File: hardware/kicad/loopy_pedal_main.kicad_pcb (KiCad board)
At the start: 2 copper layers, 80 x 66 mm, 76 parts, among them J1 USB_C_Receptacle_USB2.0_16P, J10 Conn_01x02, J11 Conn_01x03, J2 Barrel_Jack, J3 Conn_01x06, J4 Conn_01x06, J5 Conn_01x08, J6 Conn_02x03_Odd_Even, J7 Conn_02x03_Odd_Even, J8 DIN-5_180degree, J9 DIN-5_180degree, Q1 AO3401A, SW1 SW_Push, SW2 SW_Push, U1 ATmega328P-A, U10 74AHCT1G08, U2 ATmega16U2-A, U3 AP63203WU, U4 74AHCT1G125, U5 LM66100DCK, U6 LM66100DCK, U7 USBLC6-2SC6, U8 74AHCT1G125, U9 H11L1, Y1 16MHz, Y2 16MHz

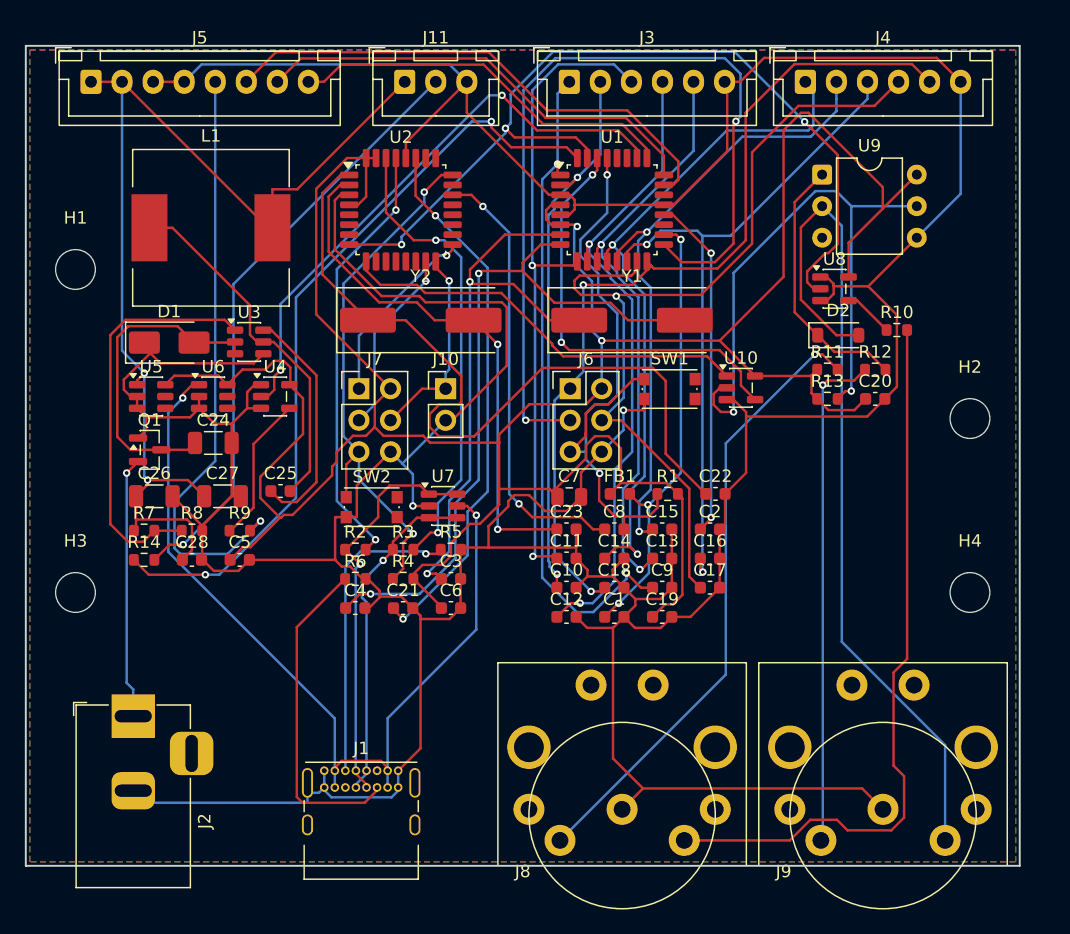
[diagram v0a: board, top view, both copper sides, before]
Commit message: fix(pcb): symmetric mounting holes, 82x66mm
Made the four M3 mounting holes a proper symmetric rectangle (74x26mm) instead
of the asymmetric set (a corner hole had been nudged to dodge the opto).
Widened 2mm to 82x66 to give the right-hand holes a clear column. Re-routed
clean: 0 DRC errors / 0 unrouted.
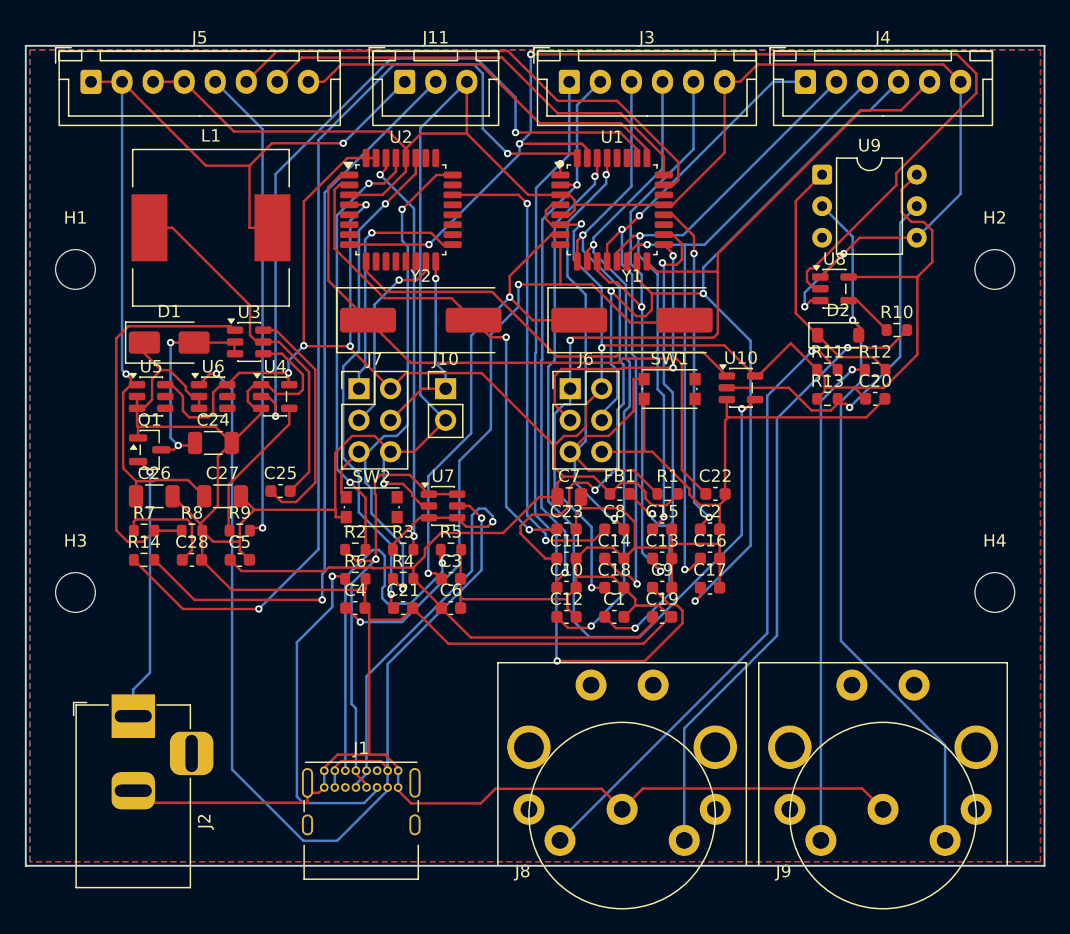
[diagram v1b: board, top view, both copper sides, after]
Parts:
- moved H2 12.2 mm to (108.0, 48.0)
- moved H4 2.00 mm to (108.0, 74.0)
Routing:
- net N$5: track 70.0 -> 24.1 mm
- net GND: track 435.9 -> 471.3 mm, vias 2 -> 3
- net UART_RX: track 34.2 -> 68.8 mm
- net UART_TX: track 71.8 -> 91.8 mm
- net MIDI_IN_OPTO: track 49.4 -> 29.8 mm, vias 2 -> 1
- net IND_DATA: track 62.3 -> 80.5 mm
- net RING_DATA: track 46.6 -> 60.2 mm
- net VBUS: track 71.2 -> 84.7 mm
- net IND_DATA_OUT: track 48.5 -> 60.3 mm
- net N$21: track 69.2 -> 57.9 mm, vias 0 -> 1
- net SW_RECPLAY: track 53.9 -> 64.9 mm
- net USB_D-: track 27.3 -> 38.2 mm
- net +5V: track 236.0 -> 225.6 mm, vias 2 -> 6
- net N$7: track 62.4 -> 52.4 mm
- net RING_DATA_OUT: track 48.3 -> 38.6 mm
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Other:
- board size 80 x 66 mm -> 82 x 66 mm
